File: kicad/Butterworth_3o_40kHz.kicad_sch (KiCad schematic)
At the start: 28 parts, among them J2 Conn_01x02_Pin, J2_SW2 Conn_01x02_Pin, J3 Conn_01x02_Pin, J4 Barrel_Jack, J5_Power1 Conn_01x02_Pin, J8_LED1 Conn_01x02_Pin, SW1 SW_DPDT_x2, SW2 SW_SPST, U1 TL072, U2 LM317L_TO92, U3 LMC7660

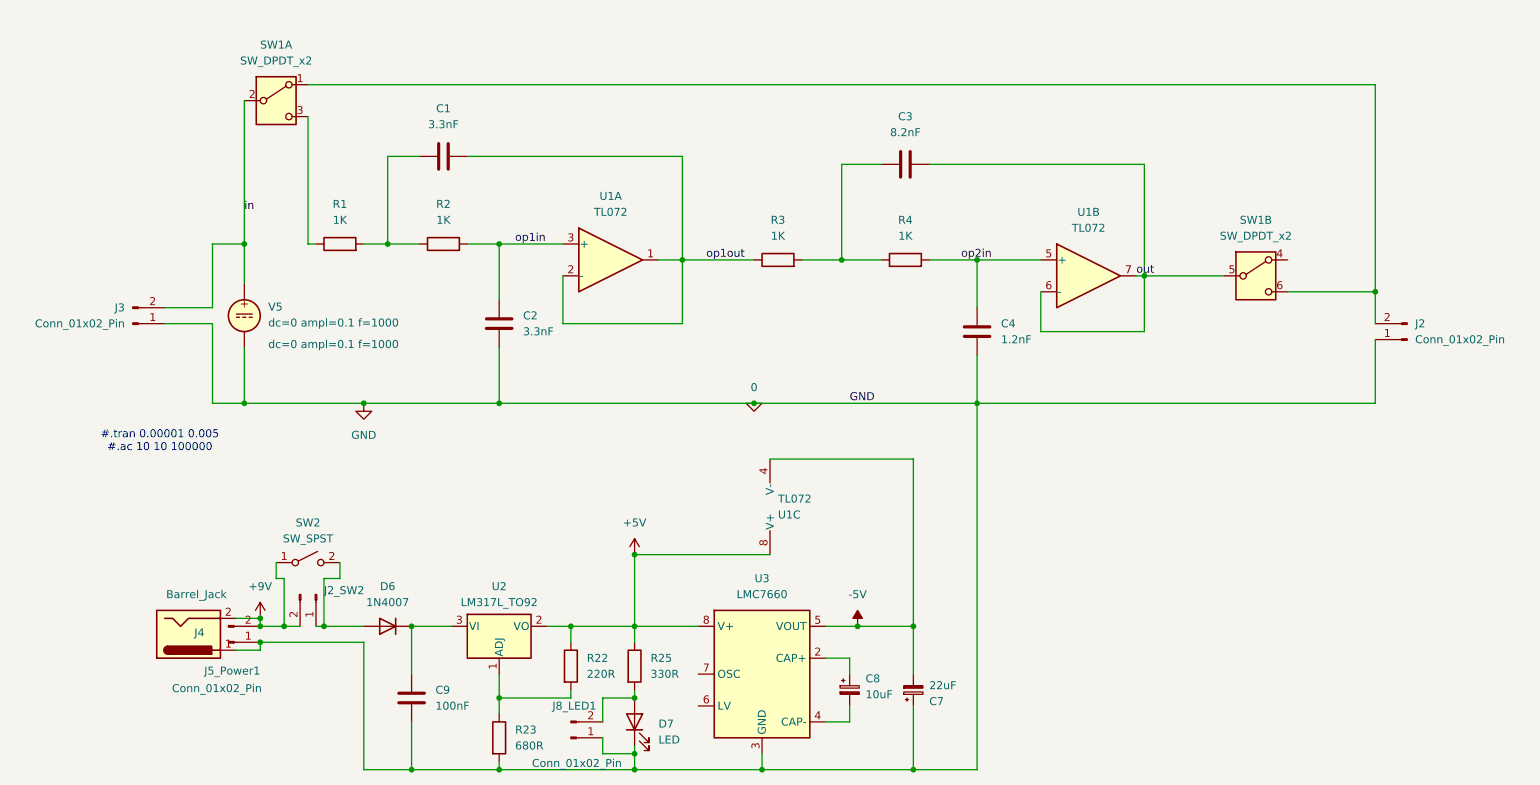
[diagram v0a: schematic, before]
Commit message: Added PDF schematic and BOM
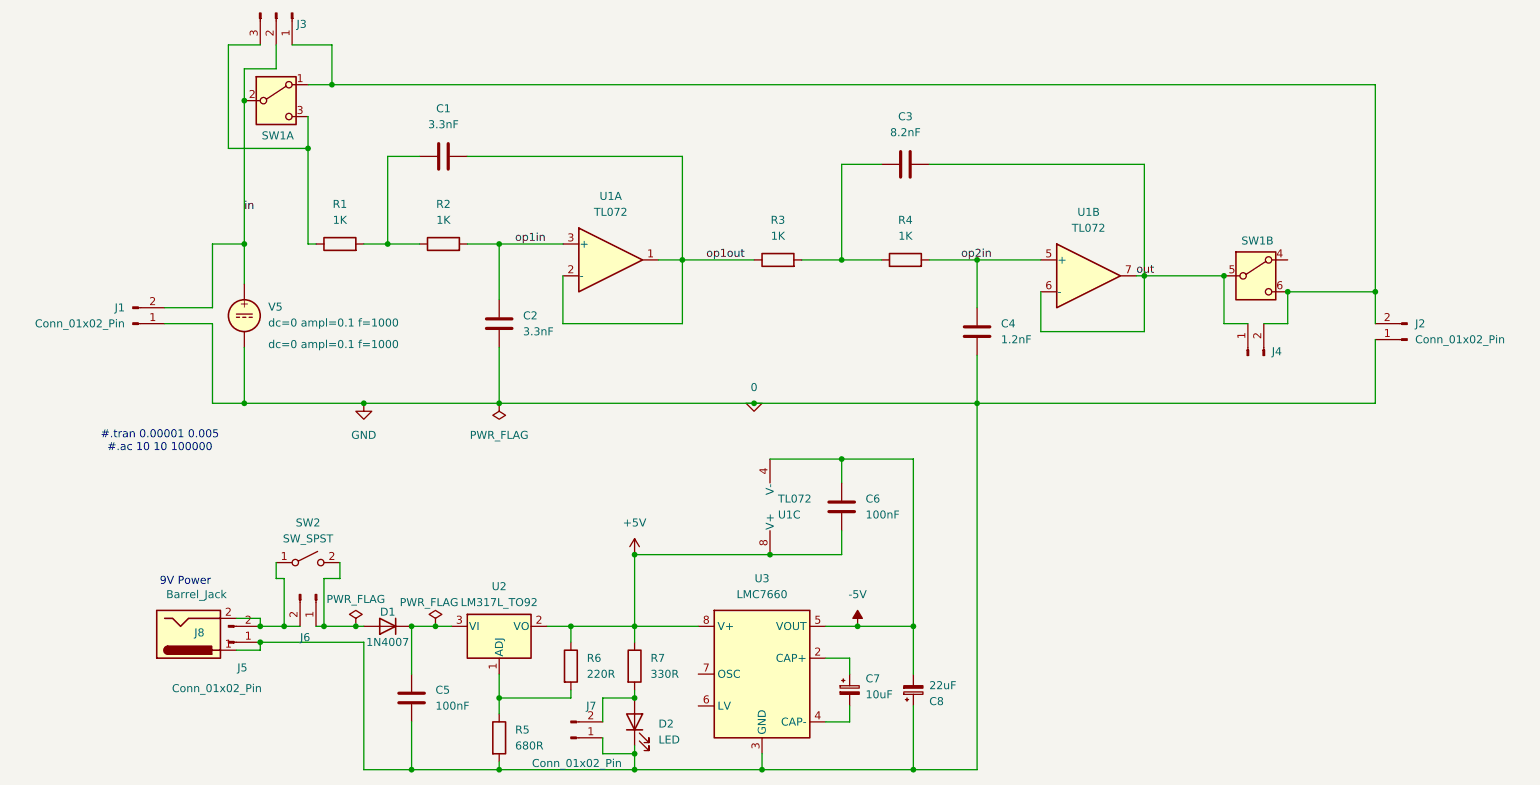
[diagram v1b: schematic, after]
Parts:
- added C6: 100nF, Capacitor_THT:C_Rect_L7.0mm_W3.5mm_P5.00mm, symbol Device:C
- added J3: Conn_01x03_Pin, Connector_Molex:Molex_KK-254_AE-6410-03A_1x03_P2.54mm_Vertical, symbol Connector:Conn_01x03_Pin
- added J4: Conn_01x02_Pin, Connector_Molex:Molex_KK-254_AE-6410-02A_1x02_P2.54mm_Vertical, symbol Connector:Conn_01x02_Pin
- C1, C2, C3, C4: footprint (none) -> Capacitor_THT:C_Rect_L7.0mm_W3.5mm_P5.00mm
- D1: renamed from D6; footprint Diode_THT:D_DO-41_SOD81_P10.16mm_Horizontal -> Diode_THT:D_DO-35_SOD27_P2.54mm_Vertical_AnodeUp
- J1: renamed from J3; footprint (none) -> Connector_Molex:Molex_KK-254_AE-6410-02A_1x02_P2.54mm_Vertical
- J2: footprint (none) -> Connector_Molex:Molex_KK-254_AE-6410-02A_1x02_P2.54mm_Vertical
- R1: footprint (none) -> Resistor_THT:R_Axial_DIN0207_L6.3mm_D2.5mm_P2.54mm_Vertical
- R2, R3, R4: footprint (none) -> Resistor_THT:R_Axial_DIN0207_L6.3mm_D2.5mm_P10.16mm_Horizontal
- U1: footprint (none) -> Package_DIP:DIP-8_W7.62mm
- U3: footprint Package_DIP:CERDIP-8_W7.62mm_SideBrazed -> Package_DIP:DIP-8_W7.62mm
- renumbered C9 to C5, C8 to C7, C7 to C8, D7 to D2, J5_Power1 to J5, J2_SW2 to J6, J8_LED1 to J7, J4 to J8, R23 to R5, R22 to R6, R25 to R7
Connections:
- net +5V: now also C6.2
- net -5V: now also C6.1
- net in: now also J3.2 (Pin_2)
- net out: now also J4.1 (Pin_1)
- net at R1.1, SW1.3 (C): now also J3.3 (Pin_3)
- net at J2.2 (Pin_2), SW1.1 (A), SW1.6 (C): now also J3.1 (Pin_1), J4.2 (Pin_2)
- net +9V: no longer names the net of J5.2 (Pin_2), J6.2 (Pin_2), J8.2, SW2.1 (A)
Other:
- note added: "9V Power"
